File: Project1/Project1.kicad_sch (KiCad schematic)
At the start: 9 parts, among them Q1 Q_NJFET_DGS, U1 TL084

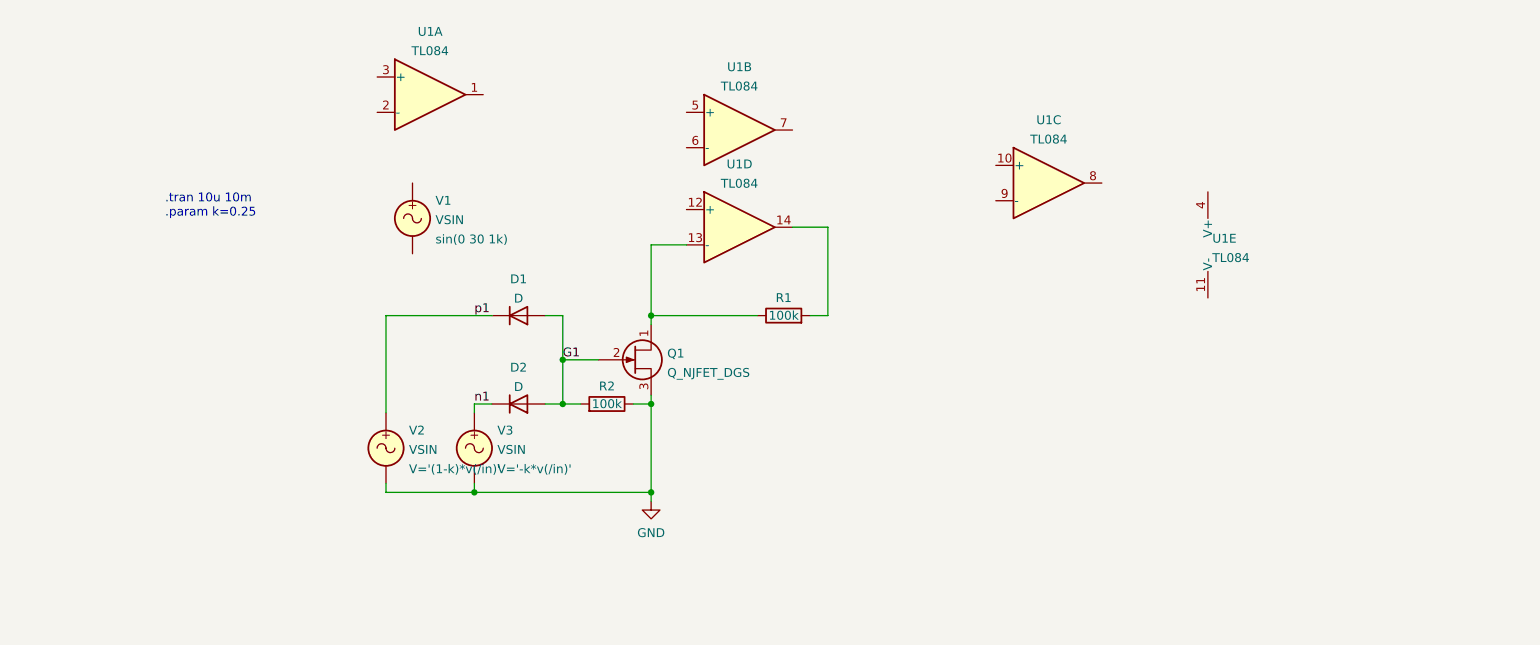
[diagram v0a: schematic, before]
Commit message: Added LM358 Spice model and implemented simple circuit
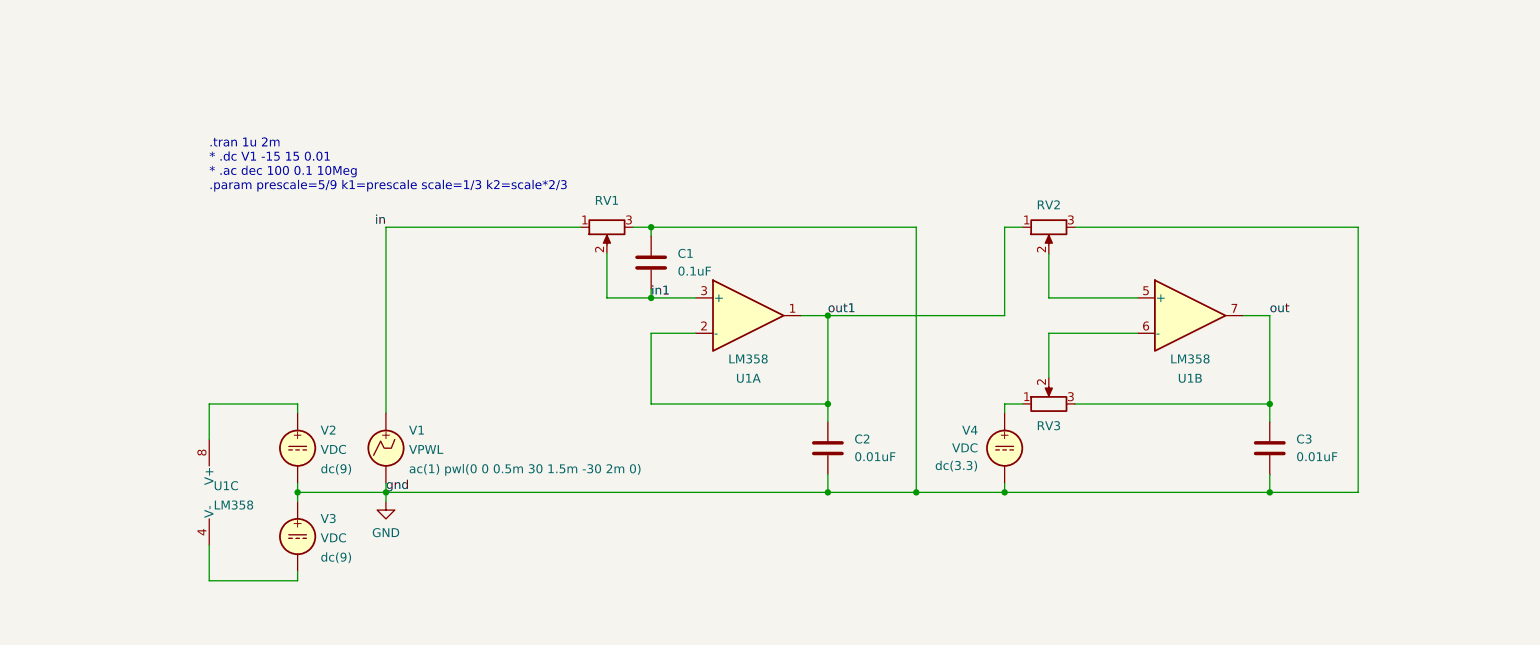
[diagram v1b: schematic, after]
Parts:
- removed D1, D2: D, symbol Device:D
- removed Q1: Q_NJFET_DGS, symbol Device:Q_NJFET_DGS
- removed R1, R2: 100k, symbol Device:R
- removed U1: TL084, symbol Amplifier_Operational:TL084
- removed V1, V2, V3: VSIN, symbol Simulation_SPICE:VSIN
- added C1: 0.1uF, symbol Device:C
- added C2, C3: 0.01uF, symbol Device:C
- added RV1, RV2, RV3: R_Potentiometer, symbol Device:R_Potentiometer
- added U1: LM358, symbol Amplifier_Operational:LM358
- added V1: VPWL, symbol Simulation_SPICE:VPWL
- added V2, V3, V4: VDC, symbol Simulation_SPICE:VDC
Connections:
- net GND: now also C1.2, C2.1, C3.1, RV1.3, RV2.3, V1.2, V2.2, V3.1, V4.2
- new net: U1.4 (V-), V3.2
- new net: U1.8 (V+), V2.1
- new net: RV3.1, V4.1
- new net: RV2.2, U1.5 (+)
- new net: RV3.2, U1.6 (-)
- new net in: RV1.1, V1.1
- new net in1: C1.1, RV1.2, U1.3 (+)
- new net out: C3.2, RV3.3, U1.7
- new net out1: C2.2, RV2.1, U1.1, U1.2 (-)
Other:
- note added: ".tran 1u 2m * .dc V1 -15 15 0.01 * .ac dec 100 0.1 10Meg .param prescale=5/9 k1=prescale scale=1/3 k2=scale*2/3"
- note removed: ".tran 10u 10m .param k=0.25"

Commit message: Added NE555 and made voltage measurement sheet
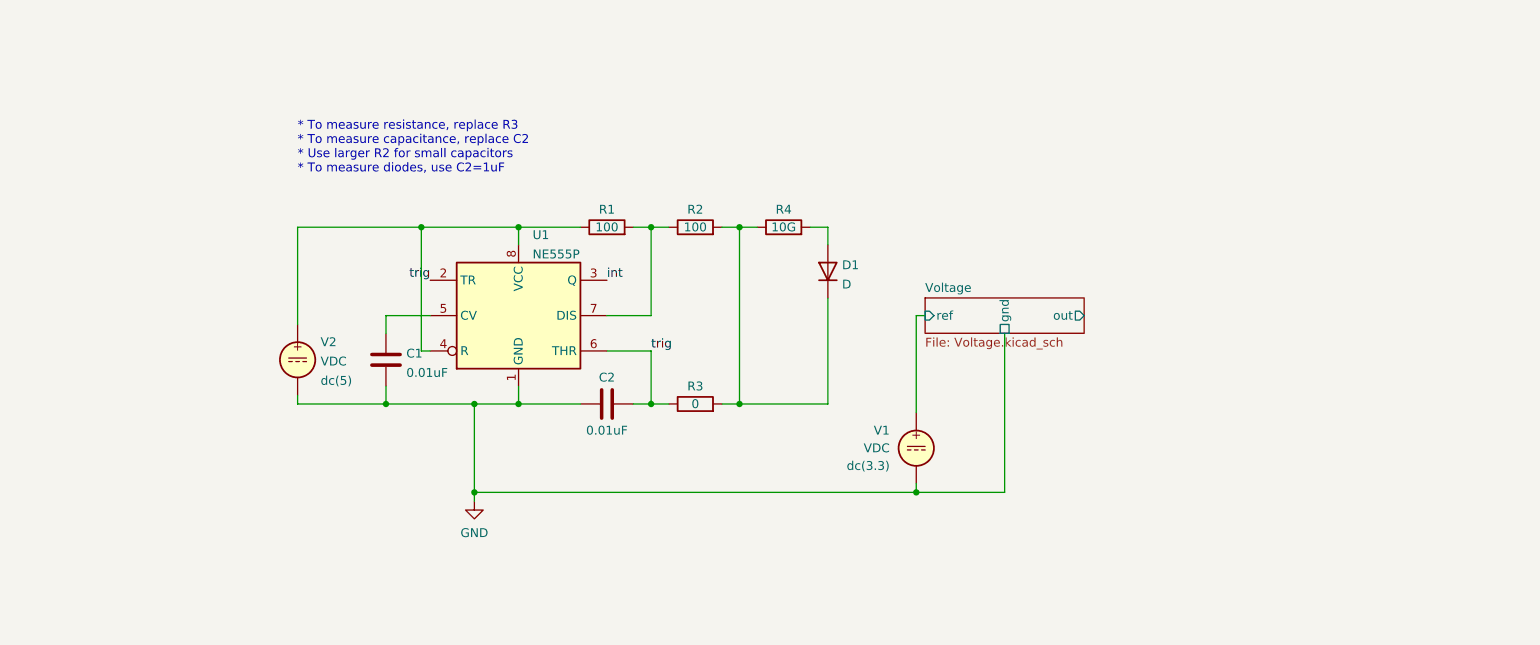
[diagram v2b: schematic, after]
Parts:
- removed C3: 0.01uF, symbol Device:C
- removed RV1, RV2, RV3: R_Potentiometer, symbol Device:R_Potentiometer
- removed U1: LM358, symbol Amplifier_Operational:LM358
- removed V1: VPWL, symbol Simulation_SPICE:VPWL
- removed V3, V4: VDC, symbol Simulation_SPICE:VDC
- added D1: D, symbol Device:D
- added R1, R2: 100, symbol Device:R
- added R3: 0, symbol Device:R
- added R4: 10G, symbol Device:R
- added U1: NE555P, Package_DIP:DIP-8_W7.62mm, symbol Timer:NE555P
- added V1: VDC, symbol Simulation_SPICE:VDC
- C1: value 0.1uF -> 0.01uF
- V2: Spice_Model dc(9) -> dc(5)
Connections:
- net GND: now also U1.1 (GND), V1.2
- net at V2.1: now also R1.1, U1.4 (R), U1.8 (VCC)
- net in1: no longer names the net of C1.1
- net in1: now also U1.5 (CV)
- net out1 renamed trig
- net trig: now also R3.1, U1.2 (TR), U1.6 (THR)
- new net: R1.2, R2.1, U1.7 (DIS)
- new net: D1.1 (K), R2.2, R3.2, R4.1
- new net: D1.2 (A), R4.2
- new net Voltage/ref: V1.1
- new net int: U1.3 (Q)
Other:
- added sheet Voltage (Voltage.kicad_sch)
- note added: "* To measure resistance, replace R3 * To measure capacitance, replace C2 * Use larger R2 for small capacitors * To measure diodes, use C2=1uF"
- note removed: ".tran 1u 2m * .dc V1 -15 15 0.01 * .ac dec 100 0.1 10Meg .param prescale=5/9 k1=prescale scale=1/3 k2=scale*2/3"

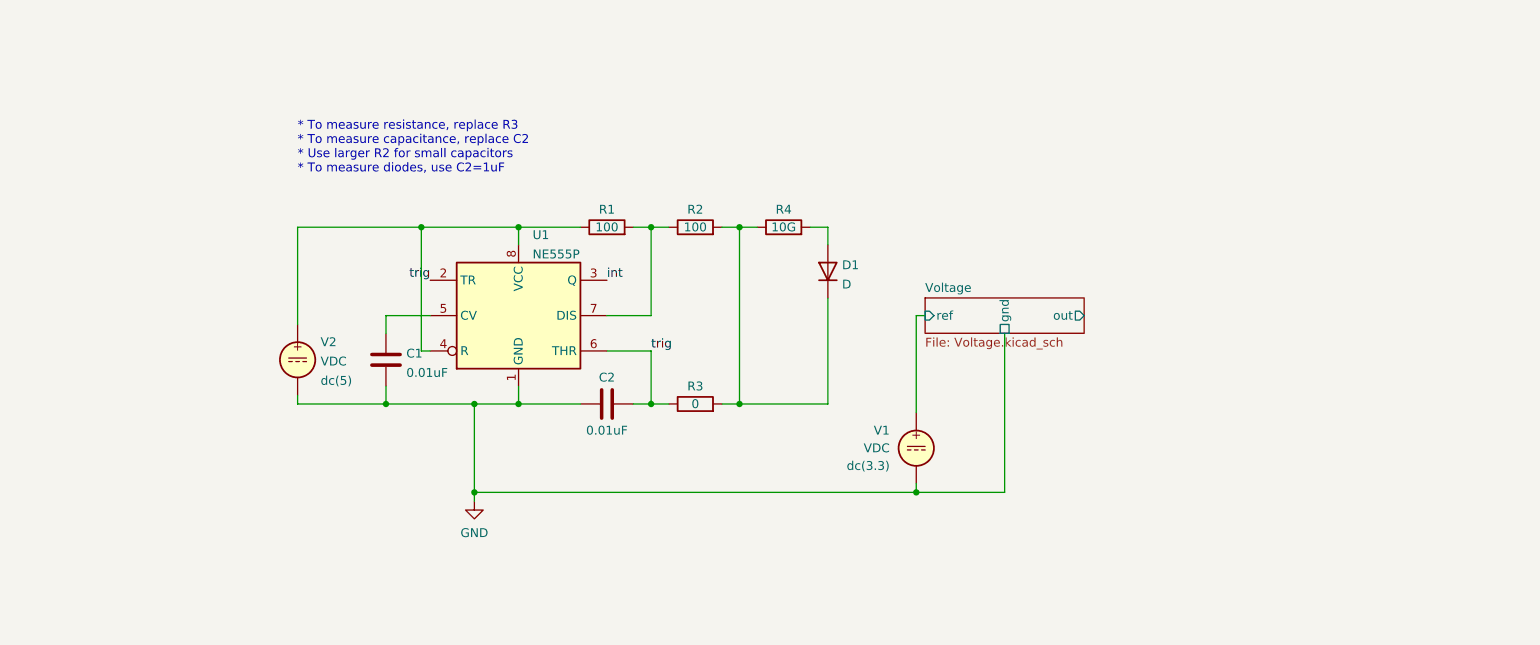
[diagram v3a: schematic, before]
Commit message: Added switches, jumpers, and header
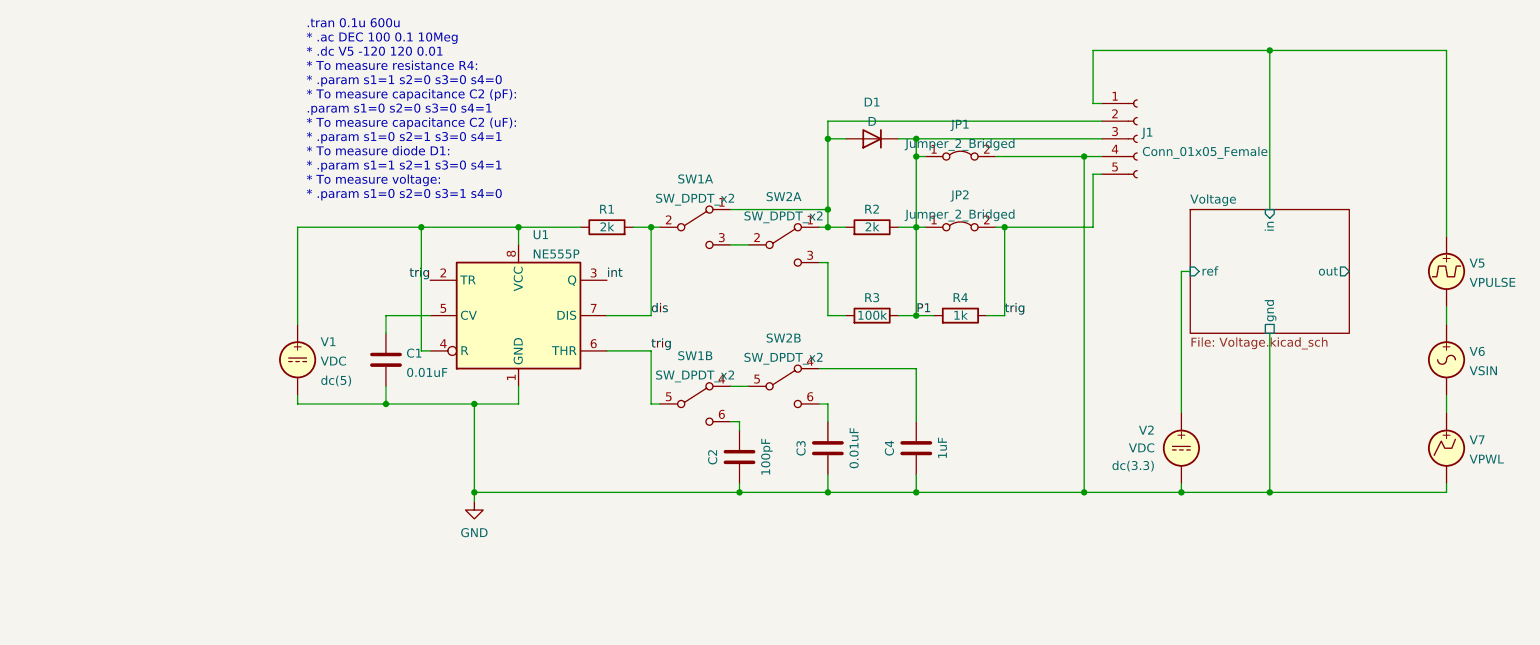
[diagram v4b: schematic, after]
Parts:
- added C2: 100pF, symbol Device:C
- added C4: 1uF, symbol Device:C
- added J1: Conn_01x05_Female, symbol Connector:Conn_01x05_Female
- added JP1, JP2: Jumper_2_Bridged, symbol Jumper:Jumper_2_Bridged
- added SW1, SW2: SW_DPDT_x2, symbol Switch:SW_DPDT_x2
- added V5: VPULSE, symbol Simulation_SPICE:VPULSE
- added V6: VSIN, symbol Simulation_SPICE:VSIN
- added V7: VPWL, symbol Simulation_SPICE:VPWL
- D1: Spice_Netlist_Enabled Y -> N; now left out of the parts list
- R1, R2: value 100 -> 2k
- R3: value 0 -> 100k
- R4: value 10G -> 1k; now left out of the parts list
- renumbered C2 to C3, V2 to V1, V1 to V2
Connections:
- net GND: now also C2.2, C4.1, J1.4 (Pin_4), JP1.2 (B), V7.2
- net trig: now also R4.1, J1.5 (Pin_5), JP2.2 (B), SW1.5 (B); no longer C3.2, R3.1
- net dis: now reaches R1.2, U1.7 (DIS)
- net dis: now also SW1.2 (B); no longer R2.1
- net at D1.2 (A): now also R2.2, J1.2 (Pin_2), SW1.1 (A), SW2.1 (A); no longer R4.2
- new net: V6.2, V7.1
- new net: C3.2, SW2.6 (C)
- new net: R3.2, SW2.3 (C)
- new net: SW1.4 (A), SW2.5 (B)
- new net: C2.1, SW1.6 (C)
- new net: V5.2, V6.1
- new net: SW1.3 (C), SW2.2 (B)
- new net: C4.2, SW2.4 (A)
- new net P1: D1.1 (K), J1.3 (Pin_3), JP1.1 (A), JP2.1 (A), R2.1, R3.1, R4.2
- new net Voltage/in: J1.1 (Pin_1), V5.1
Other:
- sheet Voltage ports: added in; removed none
- note added: ".tran 0.1u 600u * .ac DEC 100 0.1 10Meg * .dc V5 -120 120 0.01 * To measure resistance R4: * .param s1=1 s2=0 s3=0 s4=0 * To measure capacitance C2 (pF): .param s1=0 s2=0 s3=0 s4=1 * To measure capacitance C2 (uF): * .param s1=0 s2=1 s3=0 s4=1 * To measure diode D1: * .param s1=1 s2=1 s3=0 s4=1 * To measure voltage: * .param s1=0 s2=0 s3=1 s4=0"
- note removed: "* To measure resistance, replace R3 * To measure capacitance, replace C2 * Use larger R2 for small capacitors * To measure diodes, use C2=1uF"
- moved on the sheet: C3, R2, V2

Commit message: Added protective diodes and centered circuit
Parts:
- added D2, D3: D, symbol Device:D
- C2: value 100pF -> 10uF
- renumbered V5 to V3, V6 to V4, V7 to V5
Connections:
- net GND: now also D3.2 (A)
- net Voltage/out: now also D2.2 (A), D3.1 (K)
- net Voltage/ref: now also D2.1 (K)
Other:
- note added: ".tran 0.1u 600u * .tran 10u 20m *.tran 10u 200m * .ac DEC 100 0.1 10Meg * .dc V5 -120 120 0.01 * To measure resistance R4: * .param s1=1 s2=0 s3=0 s4=0 * To measure capacitance C2 (pF): * .param s1=0 s2=0 s3=0 s4=1 * To measure capacitance C2 (uF): * .param s1=0 s2=1 s3=0 s4=1 * To measure diode D1: * .param s1=1 s2=1 s3=0 s4=1 * To measure voltage: .param s1=0 s2=0 s3=1 s4=0"
- note removed: ".tran 0.1u 600u * .ac DEC 100 0.1 10Meg * .dc V5 -120 120 0.01 * To measure resistance R4: * .param s1=1 s2=0 s3=0 s4=0 * To measure capacitance C2 (pF): .param s1=0 s2=0 s3=0 s4=1 * To measure capacitance C2 (uF): * .param s1=0 s2=1 s3=0 s4=1 * To measure diode D1: * .param s1=1 s2=1 s3=0 s4=1 * To measure voltage: * .param s1=0 s2=0 s3=1 s4=0"
- moved on the sheet: C1, C2, C3, C4, D1, J1, JP1, JP2, R1, R2, R3, R4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

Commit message: Added headers for ADC and power
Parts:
- removed V1, V2: VDC, symbol Simulation_SPICE:VDC
- added J1: POWER, symbol Connector:Conn_01x04_Male
- added J3: ADC, symbol Connector:Conn_01x03_Male
- J2: renamed from J1; value Conn_01x05_Female -> INPUT
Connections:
- net GND: now also J1.3 (Pin_3), J3.1 (Pin_1), J3.3 (Pin_3)
- net Voltage/out: now also J3.2 (Pin_2)
- net VCC: now reaches R1.1, U1.4 (R), U1.8 (VCC)
- net VCC: now also J1.1 (Pin_1)
- net Voltage/ref renamed VDD
- net VDD: now also J1.2 (Pin_2)
- new net VEE: J1.4 (Pin_4)
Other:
- sheet Voltage ports: added vcc, vee; removed none
